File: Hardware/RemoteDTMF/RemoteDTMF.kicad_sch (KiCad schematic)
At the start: 27 parts, among them J1 REG. 7V, J10 MT8870D, J2 BATT 12V, J3 P12V, J4 Analog, J5 Digital, J6 TRX TELCO, J7 AL. ATTINY85, J8 IO ATTINY85, J9 AT-D578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

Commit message: Update schematic, add PCB and Gerber
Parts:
- added H1, H2, H3, H4: MountingHole_Pad, MountingHole:MountingHole_3.2mm_M3_DIN965_Pad, symbol Mechanical:MountingHole_Pad
- added unit 3 of U3
- added unit 4 of U3
- C1, C2, C3, C4: footprint (none) -> Capacitor_THT:CP_Radial_D5.0mm_P2.50mm
- C5, C6, C7: footprint (none) -> Capacitor_THT:C_Rect_L7.0mm_W3.5mm_P5.00mm
- J1, J6: footprint (none) -> Connector_PinHeader_2.54mm:PinHeader_1x04_P2.54mm_Vertical
- J10: footprint (none) -> Connector_PinHeader_2.54mm:PinHeader_1x09_P2.54mm_Vertical
- J2: footprint (none) -> TerminalBlock:TerminalBlock_MaiXu_MX126-5.0-02P_1x02_P5.00mm
- J3: footprint (none) -> Connector_PinHeader_2.54mm:PinHeader_1x01_P2.54mm_Vertical
- J7: footprint (none) -> Connector_PinHeader_2.54mm:PinHeader_1x03_P2.54mm_Vertical
- J8: footprint (none) -> Connector_PinHeader_2.54mm:PinHeader_1x06_P2.54mm_Vertical
- J9: footprint (none) -> Connector_RJ:RJ45_Amphenol_54602-x08_Horizontal
- R1, R2, R3, R4, R5, R6, R7: footprint (none) -> Resistor_THT:R_Axial_DIN0204_L3.6mm_D1.6mm_P7.62mm_Horizontal
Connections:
- net GND: now also H1.1, H2.1, H3.1, H4.1
- no-connect marks 15 -> 19

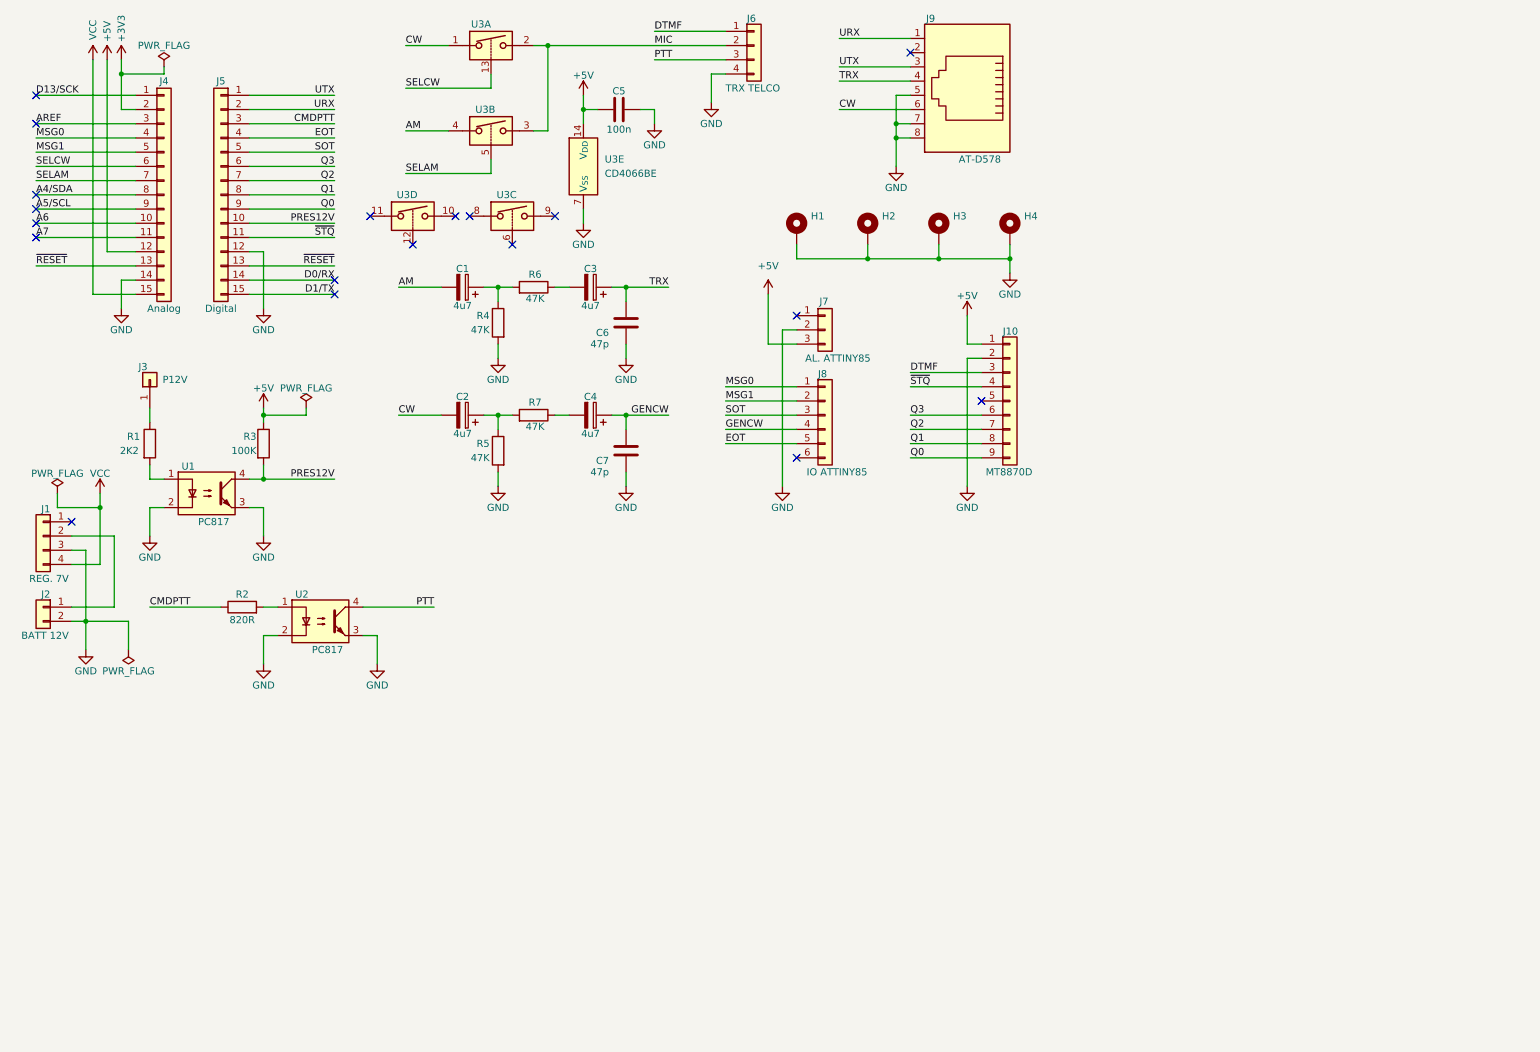
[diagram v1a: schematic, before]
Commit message: Comment Schematic, add PDF
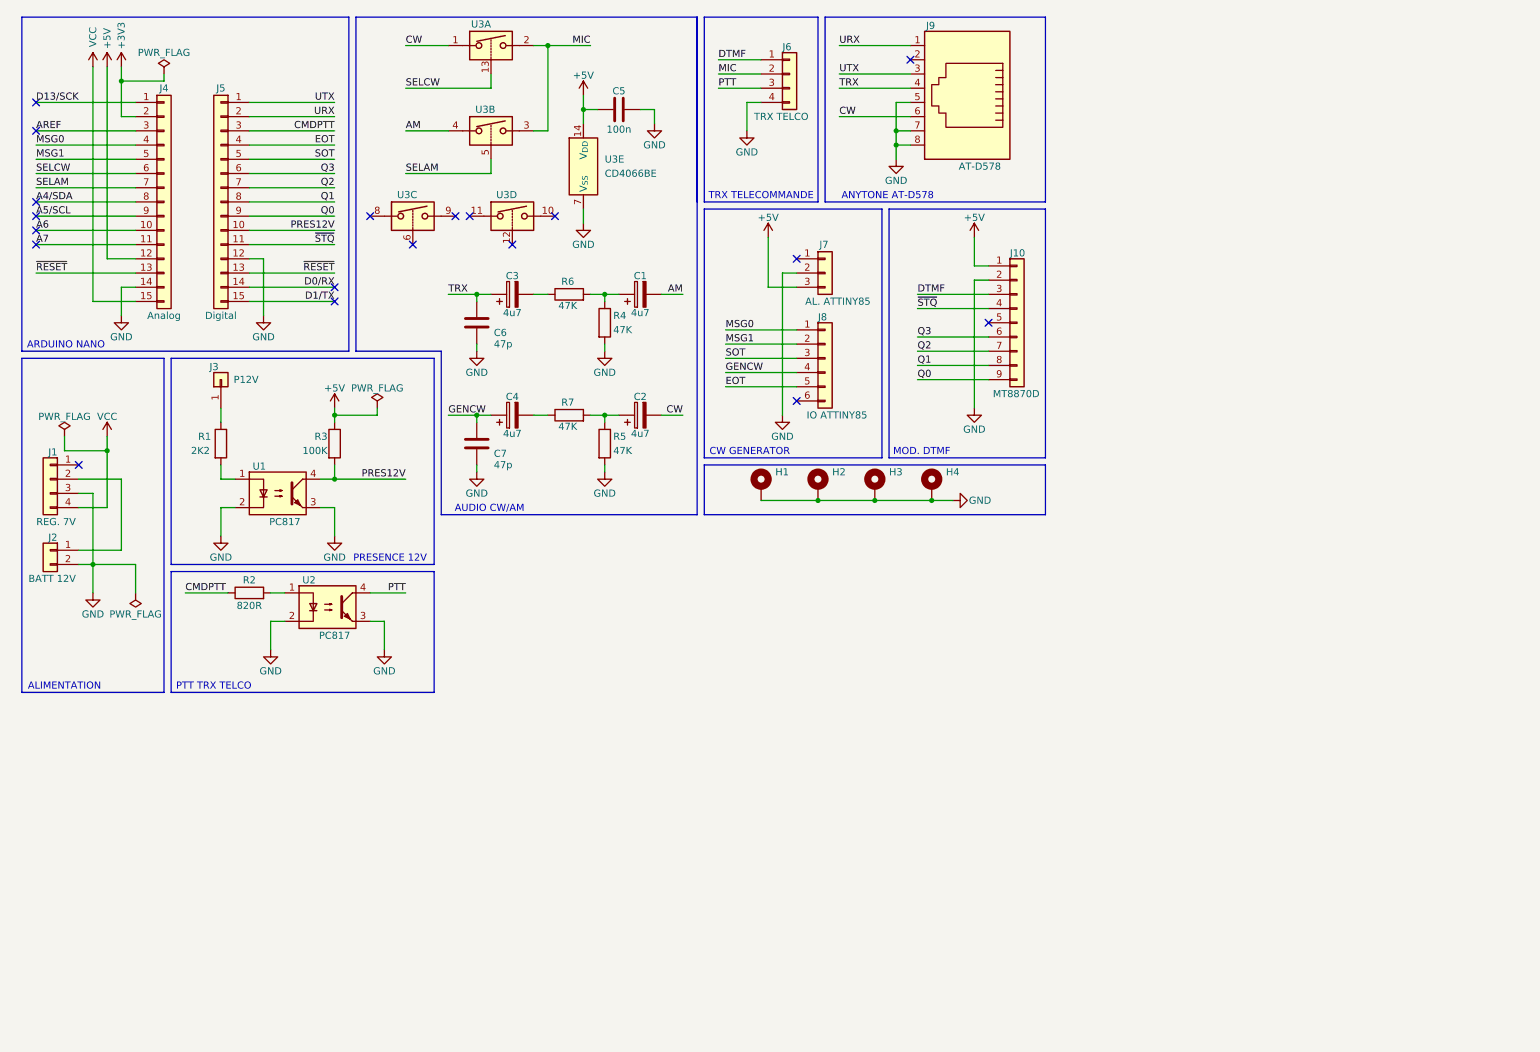
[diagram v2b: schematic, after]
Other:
- note added: "ALIMENTATION"
- note added: "ANYTONE AT-D578"
- note added: "ARDUINO NANO"
- note added: "AUDIO CW/AM"
- note added: "CW GENERATOR"
- note added: "MOD. DTMF"
- note added: "PRESENCE 12V"
- note added: "PTT TRX TELCO"
- note added: "TRX TELECOMMANDE"
- moved on the sheet: C1, C2, C3, C4, C6, C7, H1, H2, H3, H4, J1, J10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

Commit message: WIP 0.6A & Schematic
- Support D578 microphone ACK
- Update schematic
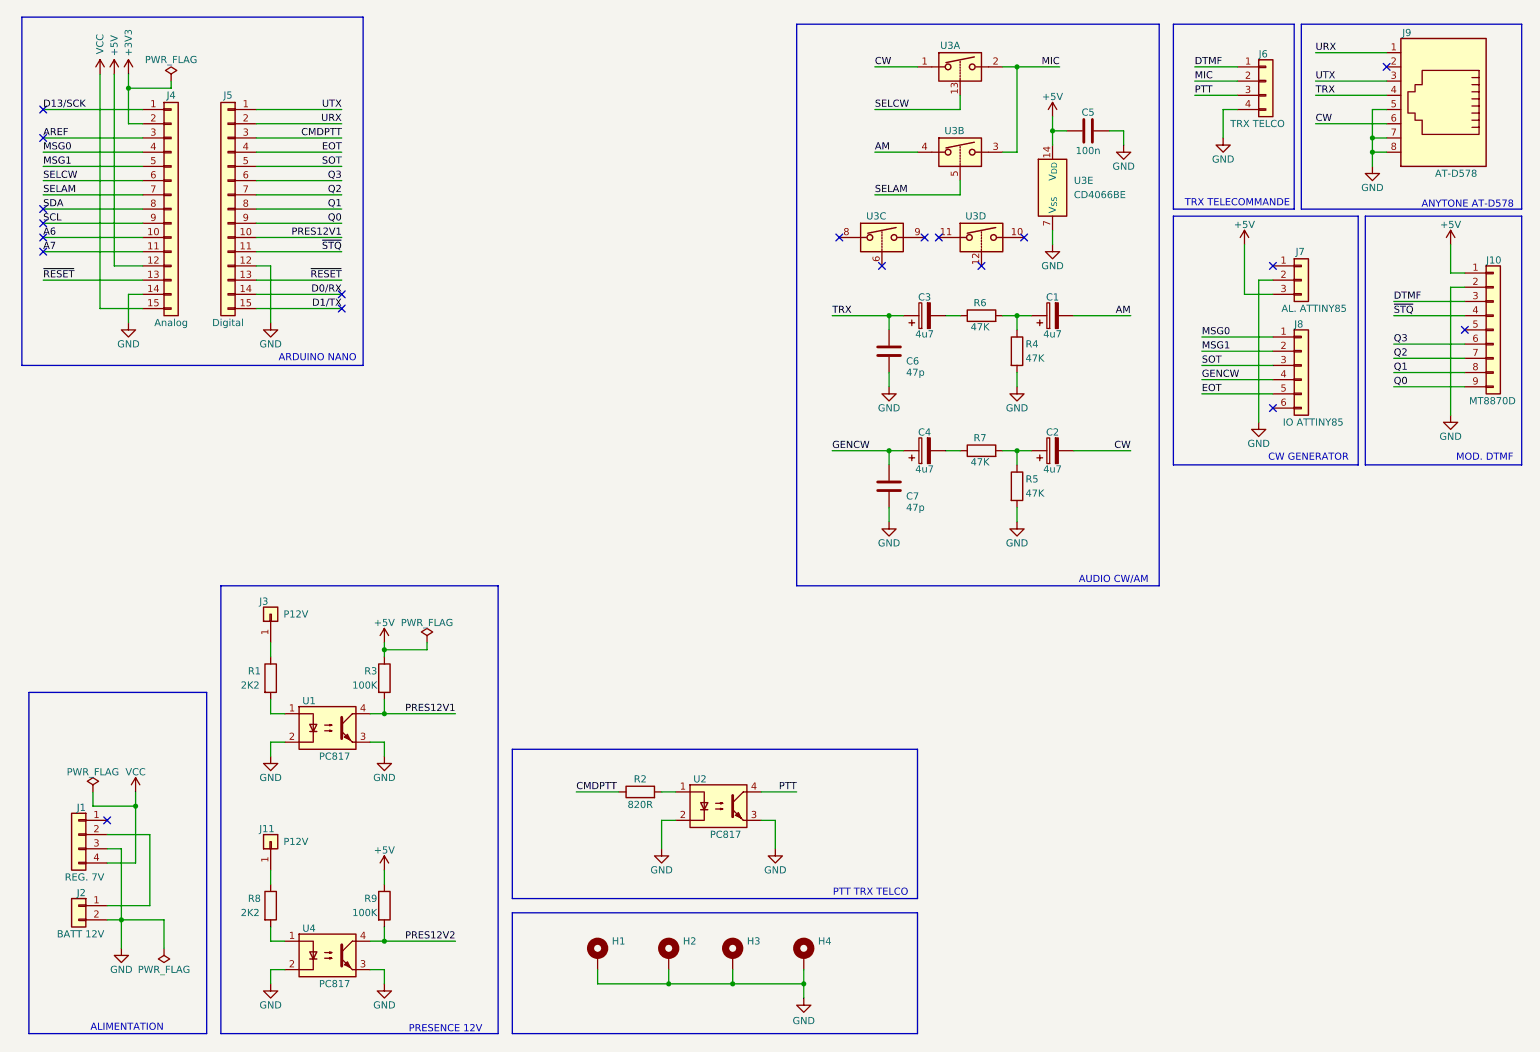
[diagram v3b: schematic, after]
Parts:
- added J11: P12V, Connector_PinHeader_2.54mm:PinHeader_1x01_P2.54mm_Vertical, symbol Connector_Generic:Conn_01x01
- added R8: 2K2, Resistor_THT:R_Axial_DIN0204_L3.6mm_D1.6mm_P7.62mm_Horizontal, symbol Device:R
- added R9: 100K, Resistor_THT:R_Axial_DIN0204_L3.6mm_D1.6mm_P7.62mm_Horizontal, symbol Device:R
- added U4: PC817, Package_DIP:DIP-4_W7.62mm, symbol Isolator:PC817
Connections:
- net +5V: now also R9.1
- net GND: now also U4.2, U4.3
- net A4/SDA renamed SDA
- net A5/SCL renamed SCL
- net PRES12V renamed PRES12V1
- new net: J11.1 (Pin_1), R8.1
- new net: R8.2, U4.1
- new net PRES12V2: R9.2, U4.4
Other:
- moved on the sheet: C1, C2, C3, C4, C5, C6, C7, H1, H2, H3, H4, J1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

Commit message: Update Schematic & WIP 0.6A
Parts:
- added D1, D2: LED, LED_THT:LED_D3.0mm, symbol Device:LED
- added J12: RELAY 1, TerminalBlock:TerminalBlock_MaiXu_MX126-5.0-02P_1x02_P5.00mm, symbol Connector_Generic:Conn_01x02
- added J13: RELAY 2, TerminalBlock:TerminalBlock_MaiXu_MX126-5.0-02P_1x02_P5.00mm, symbol Connector_Generic:Conn_01x02
- added J14: P0, Connector_PinHeader_2.54mm:PinHeader_1x10_P2.54mm_Vertical, symbol Connector_Generic:Conn_01x10
- added J15: P1, Connector_PinHeader_2.54mm:PinHeader_1x10_P2.54mm_Vertical, symbol Connector_Generic:Conn_01x10
- added J16: PCF8575, Connector_PinHeader_2.54mm:PinHeader_1x05_P2.54mm_Vertical, symbol Connector_Generic:Conn_01x05
- added J17: DS3231, Connector_PinHeader_2.54mm:PinHeader_1x06_P2.54mm_Vertical, symbol Connector_Generic:Conn_01x06
- added J18, J19: BME280, Connector_PinHeader_2.54mm:PinHeader_1x04_P2.54mm_Vertical, symbol Connector_Generic:Conn_01x04
- added R10, R11: 4K7, Resistor_THT:R_Axial_DIN0204_L3.6mm_D1.6mm_P7.62mm_Horizontal, symbol Device:R
- added R12, R13: 470R, Resistor_THT:R_Axial_DIN0204_L3.6mm_D1.6mm_P7.62mm_Horizontal, symbol Device:R
- added RLY1, RLY2: G5QU-1A, Relay_THT:Relay_SPST_Omron-G5Q-1A, symbol Relay:G5Q-1A
- added U5: ULN2803A, Package_DIP:DIP-18_W7.62mm, symbol Transistor_Array:ULN2803A
- added U6: P82B715D, Package_DIP:DIP-8_W7.62mm, symbol P82B715D:P82B715D
- J11: value P12V -> P12V2
- J3: value P12V -> P12V1
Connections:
- net +5V: now also J14.2 (Pin_2), J15.2 (Pin_2), J16.2 (Pin_2), J17.5 (Pin_5), J18.1 (Pin_1), J19.1 (Pin_1), R12.1, R13.1, U5.10 (COM), U6.8 (VCC)
- net GND: now also U3.12, U3.6, D1.1 (K), D2.1 (K), J14.1 (Pin_1), J15.1 (Pin_1), J16.1 (Pin_1), J17.6 (Pin_6), J18.2 (Pin_2), J19.2 (Pin_2), U5.9 (GND), U6.4 (GND)
- net PRES12V1: now also J15.10 (Pin_10); no longer J5.10 (Pin_10)
- net PRES12V2: now also J15.9 (Pin_9)
- net SCL: now also J16.4 (Pin_4), J17.4 (Pin_4), J18.3 (Pin_3), U6.3 (SX)
- net SDA: now also J16.3 (Pin_3), J17.3 (Pin_3), J18.4 (Pin_4), U6.6 (SY)
- net ~{STQ}: now also J5.10 (Pin_10); no longer J5.11 (Pin_11)
- net P12V2: now reaches J11.1 (Pin_1), R8.1
- net P12V2: now also J13.1 (Pin_1), RLY2.3
- net P12V1: now reaches J3.1 (Pin_1), R1.1
- net P12V1: now also J12.1 (Pin_1), RLY1.3
- net CMDPTT renamed CMD_PTT
- new net: J13.2 (Pin_2), R11.1, RLY2.2
- new net: D1.2 (A), R10.2
- new net: J12.2 (Pin_2), R10.1, RLY1.2
- new net: D2.2 (A), R11.2
- new net CMD_RLY11: RLY1.1, U5.17 (O2)
- new net CMD_RLY15: RLY1.5, U5.18 (O1)
- new net CMD_RLY21: RLY2.1, U5.15 (O4)
- new net CMD_RLY25: RLY2.5, U5.16 (O3)
- new net P00: J14.3 (Pin_3), U5.1 (I1)
- new net P01: J14.4 (Pin_4), U5.2 (I2)
- new net P02: J14.5 (Pin_5), U5.3 (I3)
- new net P03: J14.6 (Pin_6), U5.4 (I4)
- new net P04: J14.7 (Pin_7), U5.5 (I5)
- new net P05: J14.8 (Pin_8), U5.6 (I6)
- new net P06: J14.9 (Pin_9), U5.7 (I7)
- new net P07: J14.10 (Pin_10), U5.8 (I8)
- new net P12: J15.8 (Pin_8)
- new net P13: J15.7 (Pin_7)
- new net P14: J15.6 (Pin_6)
- new net P15: J15.5 (Pin_5)
- new net P16: J15.4 (Pin_4)
- new net P17: J15.3 (Pin_3)
- new net SCLX: J19.3 (Pin_3), R12.2, U6.2 (LX)
- new net SDAX: J19.4 (Pin_4), R13.2, U6.7 (LY)
- new net ~{INT}: J16.5 (Pin_5), J17.2 (Pin_2), J5.11 (Pin_11)
- no-connect marks 19 -> 26
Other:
- note added: "DRIVER RELAIS"
- note added: "EXTENSION I2C"
- note added: "MODULE DTMF"
- note added: "MODULE PIO"
- note added: "MODULE RTC"
- note added: "RELAIS TRX"
- note added: "TEMPERATURE EXTERIEUR"
- note added: "TEMPERATURE INTERIEUR"
- note removed: "MOD. DTMF"
- moved on the sheet: C1, C2, C3, C4, C5, C6, C7, H1, H2, H3, H4, J1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

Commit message: WIP Update PCB 2
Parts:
- removed J11: P12V2, Connector_PinHeader_2.54mm:PinHeader_1x01_P2.54mm_Vertical, symbol Connector_Generic:Conn_01x01
- removed J3: P12V1, Connector_PinHeader_2.54mm:PinHeader_1x01_P2.54mm_Vertical, symbol Connector_Generic:Conn_01x01
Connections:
- net SCL: now also U6.6 (SY); no longer U6.3 (SX)
- net SDA: now also U6.3 (SX); no longer U6.6 (SY)
- net P12V2S: now reaches J13.2 (Pin_2), R11.1, RLY2.2
- net P12V1S: now reaches J12.2 (Pin_2), R10.1, RLY1.2
- net SCLX renamed LDA
- net LDA: now also J19.4 (Pin_4); no longer J19.3 (Pin_3)
- net SDAX renamed LCL
- net LCL: now also J19.3 (Pin_3); no longer J19.4 (Pin_4)
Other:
- moved on the sheet: R1, R3, R8, R9, U1, U4

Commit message: WIP Update PCB 3
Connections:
- net P02: no longer U5.3 (I3)
- net P03: no longer U5.4 (I4)
- net P04: no longer U5.5 (I5)
- net P05: no longer U5.6 (I6)
- net P06: no longer U5.7 (I7)
- net P07: no longer U5.8 (I8)
- net P12: now also U5.6 (I6)
- net P13: now also U5.5 (I5)
- net P14: now also U5.4 (I4)
- net P15: now also U5.3 (I3)
- net P16: now also U5.2 (I2)
- net P17: now also U5.1 (I1)
- net PRES12V1: now also J14.3 (Pin_3); no longer J15.10 (Pin_10)
- net PRES12V2: now also J14.4 (Pin_4); no longer J15.9 (Pin_9)
- removed net P00: J14.3 (Pin_3), U5.1 (I1)
- removed net P01: J14.4 (Pin_4), U5.2 (I2)
- new net P10: J15.10 (Pin_10), U5.8 (I8)
- new net P11: J15.9 (Pin_9), U5.7 (I7)
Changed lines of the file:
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@@
 	)
 	(no_connect
-		(at 71.12 170.18)
-	)
-	(no_connect
 		(at 278.13 67.31)
 	)
@@
 	)
 	(no_connect
+		(at 17.78 175.26)
+	)
+	(no_connect
 		(at 224.79 57.15)
 	)
@@
 	)
 	(no_connect
-		(at 71.12 182.88)
-	)
-	(no_connect
 		(at 54.61 116.84)
 	)
 	(no_connect
-		(at 71.12 172.72)
+		(at 17.78 187.96)
 	)
 	(no_connect
@@
 	)
 	(no_connect
-		(at 54.61 114.3)
+		(at 17.78 177.8)
 	)
 	(no_connect
-		(at 54.61 119.38)
+		(at 54.61 114.3)
 	)
 	(no_connect
-		(at 71.12 175.26)
+		(at 54.61 119.38)
 	)
 	(no_connect
-		(at 71.12 177.8)
+		(at 17.78 185.42)
 	)
 	(no_connect
@@
 	)
 	(no_connect
-		(at 71.12 180.34)
-	)
-	(no_connect
 		(at 224.79 54.61)
 	)
@@
 	)
 	(no_connect
+		(at 17.78 182.88)
+	)
+	(no_connect
+		(at 17.78 180.34)
+	)
+	(no_connect
 		(at 171.45 125.73)
 	)
@@
 		)
 	)
-	(label "PRES12V1"
+	(label "P10"
 		(at 71.12 187.96 180)
 		(effects
@@
 		)
 	)
-	(label "P03"
+	(label "P14"
 		(at 16.51 111.76 0)
 		(effects
@@
 		)
 	)
-	(label "PRES12V2"
+	(label "P11"
 		(at 71.12 185.42 180)
 		(effects
@@
 		)
 	)
-	(label "P01"
+	(label "P16"
 		(at 16.51 106.68 0)
 		(effects
@@
 		)
 	)
-	(label "P01"
+	(label "PRES12V2"
 		(at 17.78 172.72 0)
 		(effects
@@
 		)
 	)
-	(label "P00"
+	(label "PRES12V1"
 		(at 17.78 170.18 0)
 		(effects
@@
 		)
 	)
-	(label "P05"
+	(label "P12"
 		(at 16.51 116.84 0)
 		(effects
@@
 		)
 	)
-	(label "P06"
+	(label "P11"
 		(at 16.51 119.38 0)
 		(effects
@@
 		)
 	)
-	(label "P00"
+	(label "P17"
 		(at 16.51 104.14 0)
 		(effects
@@
 		)
 	)
-	(label "P02"
+	(label "P15"
 		(at 16.51 109.22 0)
 		(effects
@@
 		)
 	)
-	(label "P04"
+	(label "P13"
 		(at 16.51 114.3 0)
 		(effects
@@
 		)
 	)
-	(label "P07"
+	(label "P10"
 		(at 16.51 121.92 0)
 		(effects

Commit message: WIP Update PCB 4
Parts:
- removed U5: ULN2803A, Package_DIP:DIP-18_W7.62mm, symbol Transistor_Array:ULN2803A
- added J11: IN2, Connector_PinHeader_2.54mm:PinHeader_1x02_P2.54mm_Vertical, symbol Connector_Generic:Conn_01x02
- added J20: OUT1, Connector_PinHeader_2.54mm:PinHeader_1x02_P2.54mm_Vertical, symbol Connector_Generic:Conn_01x02
- added J21: OUT2, Connector_PinHeader_2.54mm:PinHeader_1x02_P2.54mm_Vertical, symbol Connector_Generic:Conn_01x02
- added J22: ALIM, Connector_PinHeader_2.54mm:PinHeader_1x02_P2.54mm_Vertical, symbol Connector_Generic:Conn_01x02
- added J3: IN1, Connector_PinHeader_2.54mm:PinHeader_1x02_P2.54mm_Vertical, symbol Connector_Generic:Conn_01x02
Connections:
- net P04 is gone; now on net CMD_PTT: J14.7 (Pin_7)
- net P10 is gone; now on net CMD_RLY15: J15.10 (Pin_10)
- net P11 is gone; now on net CMD_RLY11: J15.9 (Pin_9)
- net P12 is gone; now on net CMD_RLY25: J15.8 (Pin_8)
- net P13 is gone; now on net CMD_RLY21: J15.7 (Pin_7)
- net +5V: now also J22.1 (Pin_1)
- net CMD_PTT: no longer J5.3 (Pin_3)
- net CMD_RLY11: now also J3.2 (Pin_2); no longer RLY1.1
- net CMD_RLY15: now also J3.1 (Pin_1); no longer RLY1.5
- net CMD_RLY21: now also J11.2 (Pin_2); no longer RLY2.1
- net CMD_RLY25: now also J11.1 (Pin_1); no longer RLY2.5
- net GND: now also J22.2 (Pin_2)
- net MSG0: now also J14.3 (Pin_3); no longer J4.4 (Pin_4)
- net MSG1: now also J14.4 (Pin_4); no longer J4.5 (Pin_5)
- net PRES12V1: now also J4.4 (Pin_4); no longer J14.3 (Pin_3)
- net PRES12V2: now also J4.5 (Pin_5); no longer J14.4 (Pin_4)
- net P02 renamed SEL_CW
- net SEL_CW: now also U3.13
- net P03 renamed SEL_AM
- net SEL_AM: now also U3.5
- net SELAM renamed A3
- net A3: no longer U3.5
- net SELCW renamed A2
- net A2: no longer U3.13
- new net RLY1_1: J20.2 (Pin_2), RLY1.1
- new net RLY1_5: J20.1 (Pin_1), RLY1.5
- new net RLY2_1: J21.2 (Pin_2), RLY2.1
- new net RLY2_5: J21.1 (Pin_1), RLY2.5
